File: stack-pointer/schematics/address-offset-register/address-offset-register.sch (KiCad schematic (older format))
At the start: 12 parts

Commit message: more work on stack pointer
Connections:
- net GND: no longer U?.7 (C0)
- new net AP1: U?.7 (C0)
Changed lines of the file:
@@
 	1    0    0    -1
 $EndComp
-$Comp
-L common-symbols:BarGraphLED_8P BAR?
-U 1 1 615D5CEB
-P 10350 3675
-F 0 "BAR?" H 10350 4342 50  0000 C CNN
-F 1 "BarGraphLED_8P" H 10350 4251 50  0000 C CNN
-F 2 "" H 10350 3675 50  0001 C CNN
-F 3 "" H 10350 3675 50  0001 C CNN
-	1    10350 3675
-	1    0    0    -1
-$EndComp
-Wire Wire Line
-	10150 3975 10050 3975
 Connection ~ 8625 3975
 Wire Wire Line
 	8625 3975 8625 4150
-Wire Wire Line
-	10150 3875 9950 3875
 Connection ~ 8525 3875
 Wire Wire Line
 	8525 3875 8525 3225
-Wire Wire Line
-	10150 3775 9850 3775
 Connection ~ 8425 3775
 Wire Wire Line
 	8425 3775 8425 4150
-Wire Wire Line
-	10150 3675 9750 3675
 Connection ~ 8325 3675
 Wire Wire Line
 	8325 3675 8325 3225
-Wire Wire Line
-	10150 3575 9650 3575
 Connection ~ 6650 3575
 Wire Wire Line
 	6650 3575 6650 3225
-Wire Wire Line
-	10150 3475 9550 3475
 Connection ~ 6550 3475
 Wire Wire Line
 	6550 3475 6550 3225
-Wire Wire Line
-	10150 3375 9450 3375
 Connection ~ 6450 3375
 Wire Wire Line
 	6450 3375 6450 3225
-Wire Wire Line
-	10150 3275 9350 3275
 Connection ~ 6350 3275
 Wire Wire Line
@@
 Text HLabel 9450 2200 2    50   Input ~ 0
 AOa
+Wire Wire Line
+	7825 3675 7825 4150
+Wire Wire Line
+	9350 2200 9450 2200
+Wire Wire Line
+	8750 2200 8125 2200
+Connection ~ 8125 2200
+Wire Wire Line
+	6575 6025 6575 6150
+Wire Wire Line
+	6475 5950 6475 6150
+Wire Wire Line
+	6375 5875 6375 6150
+Wire Wire Line
+	6275 5800 6275 6150
+Wire Wire Line
+	6175 5725 6175 6150
+Wire Wire Line
+	6075 5650 6075 6150
+Wire Wire Line
+	5975 5575 5975 6150
+Wire Wire Line
+	5875 5500 5875 6150
+$Comp
+L power:GND #PWR?
+U 1 1 61603AA0
+P 10050 4475
+F 0 "#PWR?" H 10050 4225 50  0001 C CNN
+F 1 "GND" H 10055 4302 50  0000 C CNN
+F 2 "" H 10050 4475 50  0001 C CNN
+F 3 "" H 10050 4475 50  0001 C CNN
+	1    10050 4475
+	1    0    0    -1
+$EndComp
+Wire Wire Line
+	10050 3975 8625 3975
+Wire Wire Line
+	10150 3975 10050 3975
+Connection ~ 10050 3975
+Wire Wire Line
+	10050 4075 10050 3975
+Wire Wire Line
+	9950 3875 8525 3875
+Wire Wire Line
+	10150 3875 9950 3875
+Connection ~ 9950 3875
+Wire Wire Line
+	9950 4075 9950 3875
+Wire Wire Line
+	9850 3775 8425 3775
+Wire Wire Line
+	10150 3775 9850 3775
+Connection ~ 9850 3775
+Wire Wire Line
+	9850 4075 9850 3775
+Wire Wire Line
+	9750 3675 8325 3675
+Wire Wire Line
+	10150 3675 9750 3675
+Connection ~ 9750 3675
+Wire Wire Line
+	9750 4075 9750 3675
+Wire Wire Line
+	9650 3575 6650 3575
+Wire Wire Line
+	10150 3575 9650 3575
+Connection ~ 9650 3575
+Wire Wire Line
+	9650 4075 9650 3575
+Wire Wire Line
+	9550 3475 6550 3475
+Wire Wire Line
+	10150 3475 9550 3475
+Connection ~ 9550 3475
+Wire Wire Line
+	9550 4075 9550 3475
+Wire Wire Line
+	9450 3375 6450 3375
+Wire Wire Line
+	10150 3375 9450 3375
+Connection ~ 9450 3375
+Wire Wire Line
+	9450 4075 9450 3375
+Wire Wire Line
+	9350 3275 6350 3275
+Wire Wire Line
+	10150 3275 9350 3275
+Connection ~ 9350 3275
+Wire Wire Line
+	9350 4075 9350 3275
+$Comp
+L common-symbols:BarGraphLED_8P BAR?
+U 1 1 615D5CEB
+P 10350 3675
+F 0 "BAR?" H 10350 4342 50  0000 C CNN
+F 1 "BarGraphLED_8P" H 10350 4251 50  0000 C CNN
+F 2 "" H 10350 3675 50  0001 C CNN
+F 3 "" H 10350 3675 50  0001 C CNN
+	1    10350 3675
+	1    0    0    -1
+$EndComp
 $Comp
 L Device:R_Network08_US RN?
@@
 	-1   0    0    1
 $EndComp
-Wire Wire Line
-	10050 4075 10050 3975
-Connection ~ 10050 3975
-Wire Wire Line
-	10050 3975 8625 3975
-Wire Wire Line
-	9950 4075 9950 3875
-Connection ~ 9950 3875
-Wire Wire Line
-	9950 3875 8525 3875
-Wire Wire Line
-	9850 4075 9850 3775
-Connection ~ 9850 3775
-Wire Wire Line
-	9850 3775 8425 3775
-Wire Wire Line
-	9750 4075 9750 3675
-Connection ~ 9750 3675
-Wire Wire Line
-	9750 3675 8325 3675
-Wire Wire Line
-	9650 4075 9650 3575
-Connection ~ 9650 3575
-Wire Wire Line
-	9650 3575 6650 3575
-Wire Wire Line
-	9550 4075 9550 3475
-Connection ~ 9550 3475
-Wire Wire Line
-	9550 3475 6550 3475
-Wire Wire Line
-	9450 4075 9450 3375
-Connection ~ 9450 3375
-Wire Wire Line
-	9450 3375 6450 3375
-Wire Wire Line
-	9350 4075 9350 3275
-Connection ~ 9350 3275
-Wire Wire Line
-	9350 3275 6350 3275
-$Comp
-L power:GND #PWR?
-U 1 1 61603AA0
-P 10050 4475
-F 0 "#PWR?" H 10050 4225 50  0001 C CNN
-F 1 "GND" H 10055 4302 50  0000 C CNN
-F 2 "" H 10050 4475 50  0001 C CNN
-F 3 "" H 10050 4475 50  0001 C CNN
-	1    10050 4475
-	1    0    0    -1
-$EndComp
-Wire Wire Line
-	7825 3675 7825 4150
-Wire Wire Line
-	8825 4150 8825 4075
-Wire Wire Line
-	8825 4075 7525 4075
-Wire Wire Line
-	7525 4075 7525 4650
-Connection ~ 7525 4650
-Wire Wire Line
-	9350 2200 9450 2200
-Wire Wire Line
-	8750 2200 8125 2200
-Connection ~ 8125 2200
-Wire Wire Line
-	6575 6025 6575 6150
-Wire Wire Line
-	6475 5950 6475 6150
-Wire Wire Line
-	6375 5875 6375 6150
-Wire Wire Line
-	6275 5800 6275 6150
-Wire Wire Line
-	6175 5725 6175 6150
-Wire Wire Line
-	6075 5650 6075 6150
-Wire Wire Line
-	5975 5575 5975 6150
-Wire Wire Line
-	5875 5500 5875 6150
+Text HLabel 9450 2875 2    50   Input ~ 0
+AP1
+Wire Wire Line
+	8825 2875 9450 2875
+Wire Wire Line
+	8825 2875 8825 4150
 $EndSCHEMATC

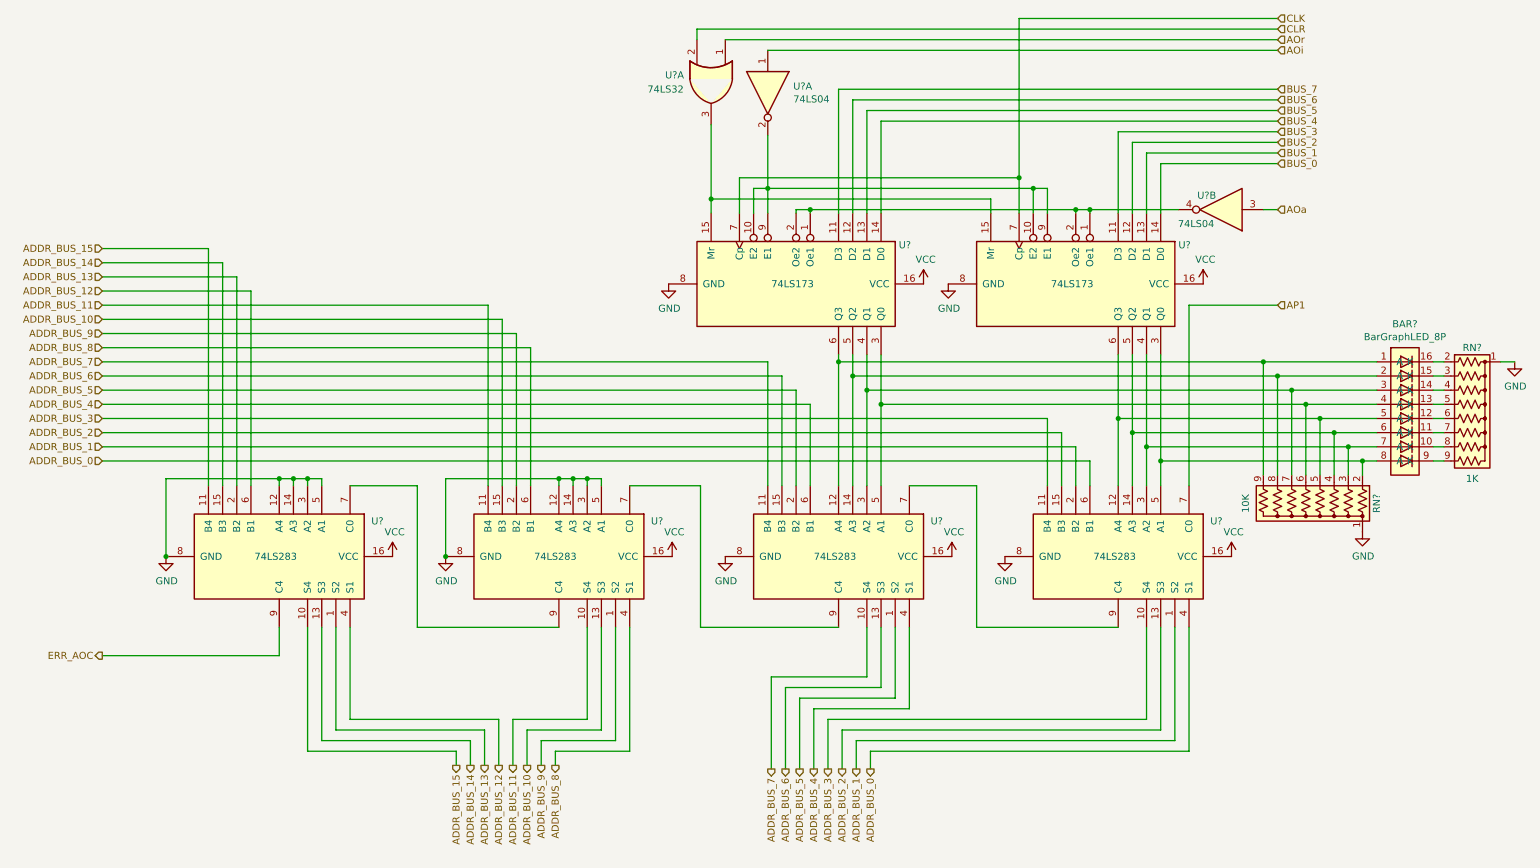
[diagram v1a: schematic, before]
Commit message: updated address bus handling and added support for halt on error
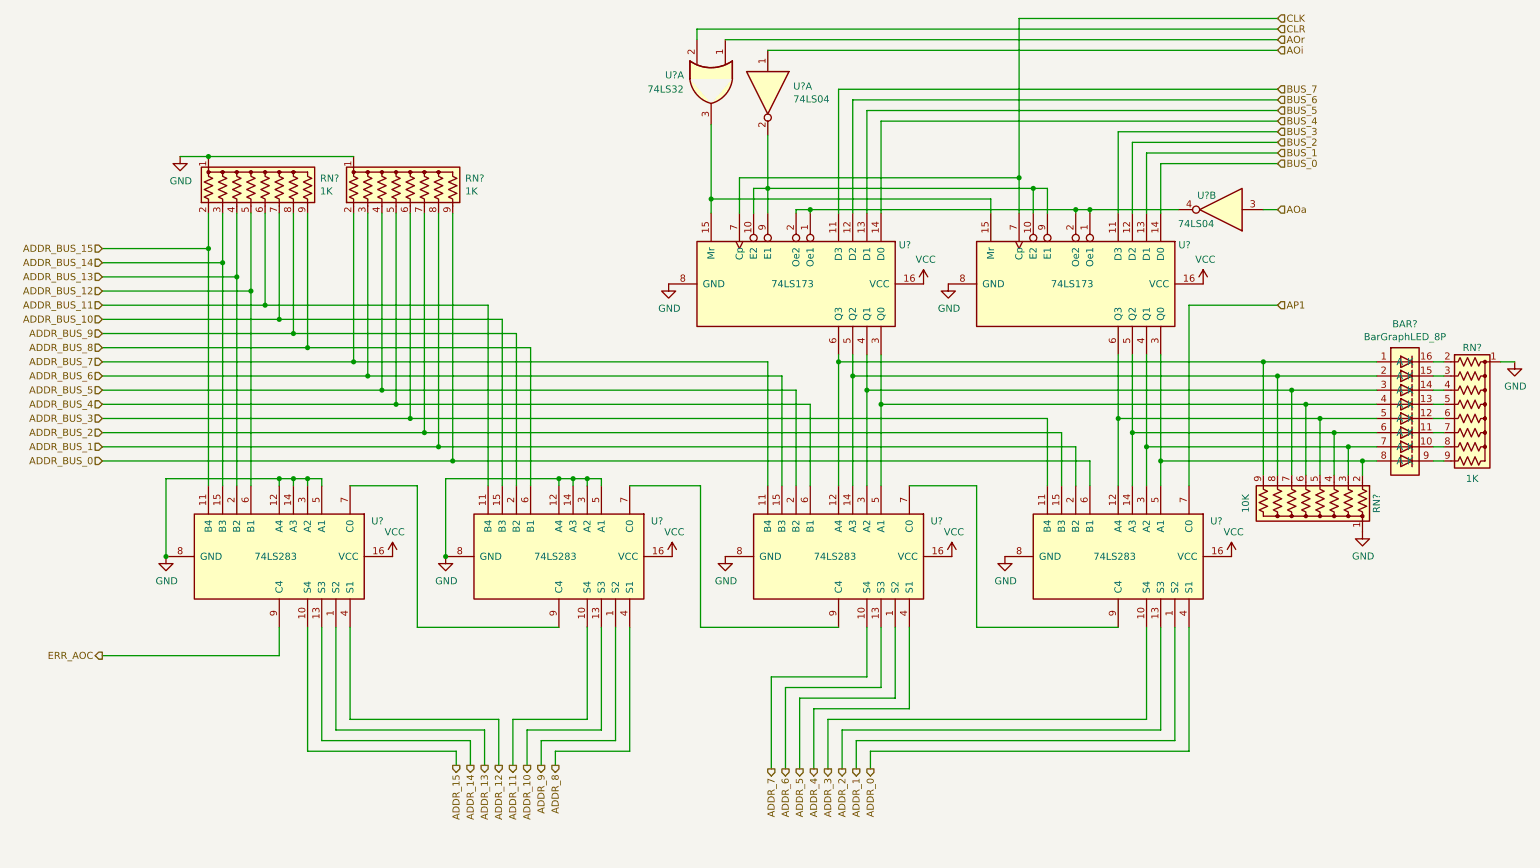
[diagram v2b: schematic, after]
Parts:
- added RN? (x2): 1K, Resistor_THT:R_Array_SIP9, symbol Device:R_Network08_US
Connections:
- net ADDR_BUS_0: now also RN?.9 (R8); no longer U?.4 (S1)
- net ADDR_BUS_1: now also RN?.8 (R7); no longer U?.1 (S2)
- net ADDR_BUS_10: now also RN?.7 (R6); no longer U?.13 (S3)
- net ADDR_BUS_11: now also RN?.6 (R5); no longer U?.10 (S4)
- net ADDR_BUS_12: now also RN?.5 (R4); no longer U?.4 (S1)
- net ADDR_BUS_13: now also RN?.4 (R3); no longer U?.1 (S2)
- net ADDR_BUS_14: now also RN?.3 (R2); no longer U?.13 (S3)
- net ADDR_BUS_15: now also RN?.2 (R1); no longer U?.10 (S4)
- net ADDR_BUS_2: now also RN?.7 (R6); no longer U?.13 (S3)
- net ADDR_BUS_3: now also RN?.6 (R5); no longer U?.10 (S4)
- net ADDR_BUS_4: now also RN?.5 (R4); no longer U?.4 (S1)
- net ADDR_BUS_5: now also RN?.4 (R3); no longer U?.1 (S2)
- net ADDR_BUS_6: now also RN?.3 (R2); no longer U?.13 (S3)
- net ADDR_BUS_7: now also RN?.2 (R1); no longer U?.10 (S4)
- net ADDR_BUS_8: now also RN?.9 (R8); no longer U?.4 (S1)
- net ADDR_BUS_9: now also RN?.8 (R7); no longer U?.1 (S2)
- net GND: now also RN?.1 (common), RN?.1 (common)
- new net ADDR_0: U?.4 (S1)
- new net ADDR_1: U?.1 (S2)
- new net ADDR_10: U?.13 (S3)
- new net ADDR_11: U?.10 (S4)
- new net ADDR_12: U?.4 (S1)
- new net ADDR_13: U?.1 (S2)
- new net ADDR_14: U?.13 (S3)
- new net ADDR_15: U?.10 (S4)
- new net ADDR_2: U?.13 (S3)
- new net ADDR_3: U?.10 (S4)
- new net ADDR_4: U?.4 (S1)
- new net ADDR_5: U?.1 (S2)
- new net ADDR_6: U?.13 (S3)
- new net ADDR_7: U?.10 (S4)
- new net ADDR_8: U?.4 (S1)
- new net ADDR_9: U?.1 (S2)
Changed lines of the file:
@@
 	6350 1350 6350 2225
 Text HLabel 6575 6150 3    50   Output ~ 0
-ADDR_BUS_0
+ADDR_0
 Text HLabel 6475 6150 3    50   Output ~ 0
-ADDR_BUS_1
+ADDR_1
 Text HLabel 6375 6150 3    50   Output ~ 0
-ADDR_BUS_2
+ADDR_2
 Text HLabel 6275 6150 3    50   Output ~ 0
-ADDR_BUS_3
+ADDR_3
 Text HLabel 6175 6150 3    50   Output ~ 0
-ADDR_BUS_4
+ADDR_4
 Text HLabel 6075 6150 3    50   Output ~ 0
-ADDR_BUS_5
+ADDR_5
 Text HLabel 5975 6150 3    50   Output ~ 0
-ADDR_BUS_6
+ADDR_6
 Text HLabel 5875 6150 3    50   Output ~ 0
-ADDR_BUS_7
+ADDR_7
 Text HLabel 4350 6125 3    50   Output ~ 0
-ADDR_BUS_8
+ADDR_8
 Text HLabel 4250 6125 3    50   Output ~ 0
-ADDR_BUS_9
+ADDR_9
 Text HLabel 4150 6125 3    50   Output ~ 0
-ADDR_BUS_10
+ADDR_10
 Text HLabel 4050 6125 3    50   Output ~ 0
-ADDR_BUS_11
+ADDR_11
 Text HLabel 3950 6125 3    50   Output ~ 0
-ADDR_BUS_12
+ADDR_12
 Text HLabel 3850 6125 3    50   Output ~ 0
-ADDR_BUS_13
+ADDR_13
 Text HLabel 3750 6125 3    50   Output ~ 0
-ADDR_BUS_14
+ADDR_14
 Text HLabel 3650 6125 3    50   Output ~ 0
-ADDR_BUS_15
+ADDR_15
 Wire Wire Line
 	4375 4150 4375 4100
@@
 ADDR_BUS_1
 Wire Wire Line
-	1150 3875 8025 3875
+	1150 3875 3525 3875
 Wire Wire Line
 	8025 3875 8025 4150
@@
 ADDR_BUS_7
 Wire Wire Line
-	1150 3975 8125 3975
+	1150 3975 3625 3975
 Wire Wire Line
 	8125 3975 8125 4150
 Wire Wire Line
-	1150 3775 7925 3775
+	1150 3775 3425 3775
 Wire Wire Line
 	7925 3775 7925 4150
 Wire Wire Line
-	1150 3675 7825 3675
-Wire Wire Line
-	1150 3575 6150 3575
+	1150 3675 3325 3675
+Wire Wire Line
+	1150 3575 3225 3575
 Wire Wire Line
 	6150 3575 6150 4150
 Wire Wire Line
-	1150 3475 6050 3475
+	1150 3475 3125 3475
 Wire Wire Line
 	6050 3475 6050 4150
 Wire Wire Line
-	1150 3375 5950 3375
+	1150 3375 3025 3375
 Wire Wire Line
 	5950 3375 5950 4150
 Wire Wire Line
-	1150 3275 5850 3275
+	1150 3275 2925 3275
 Wire Wire Line
 	5850 3275 5850 4150
@@
 ADDR_BUS_15
 Wire Wire Line
-	1150 3175 4175 3175
+	1150 3175 2600 3175
 Wire Wire Line
 	4175 3175 4175 4150
 Wire Wire Line
-	1150 3075 4075 3075
+	1150 3075 2500 3075
 Wire Wire Line
 	4075 3075 4075 4150
 Wire Wire Line
-	1150 2975 3975 2975
+	1150 2975 2400 2975
 Wire Wire Line
 	3975 2975 3975 4150
 Wire Wire Line
-	1150 2875 3875 2875
+	1150 2875 2300 2875
 Wire Wire Line
 	3875 2875 3875 4150
@@
 Wire Wire Line
 	8825 2875 8825 4150
+$Comp
+L Device:R_Network08_US RN?
+U 1 1 6161A5EE
+P 2300 2025
+F 0 "RN?" H 2688 2071 50  0000 L CNN
+F 1 "1K" H 2688 1980 50  0000 L CNN
+F 2 "Resistor_THT:R_Array_SIP9" V 2775 2025 50  0001 C CNN
+F 3 "http://www.vishay.com/docs/31509/csc.pdf" H 2300 2025 50  0001 C CNN
+	1    2300 2025
+	1    0    0    -1
+$EndComp
+$Comp
+L Device:R_Network08_US RN?
+U 1 1 6161C78B
+P 3325 2025
+F 0 "RN?" H 3713 2071 50  0000 L CNN
+F 1 "1K" H 3713 1980 50  0000 L CNN
+F 2 "Resistor_THT:R_Array_SIP9" V 3800 2025 50  0001 C CNN
+F 3 "http://www.vishay.com/docs/31509/csc.pdf" H 3325 2025 50  0001 C CNN
+	1    3325 2025
+	1    0    0    -1
+$EndComp
+Wire Wire Line
+	1900 2225 1900 2475
+Connection ~ 1900 2475
+Wire Wire Line
+	2000 2575 2000 2225
+Connection ~ 2000 2575
+Wire Wire Line
+	2100 2225 2100 2675
+Connection ~ 2100 2675
+Wire Wire Line
+	2200 2225 2200 2775
+Connection ~ 2200 2775
+Wire Wire Line
+	2300 2225 2300 2875
+Connection ~ 2300 2875
+Wire Wire Line
+	2300 2875 3875 2875
+Wire Wire Line
+	2400 2225 2400 2975
+Connection ~ 2400 2975
+Wire Wire Line
+	2400 2975 3975 2975
+Wire Wire Line
+	2500 2225 2500 3075
+Connection ~ 2500 3075
+Wire Wire Line
+	2500 3075 4075 3075
+Wire Wire Line
+	2600 2225 2600 3175
+Connection ~ 2600 3175
+Wire Wire Line
+	2600 3175 4175 3175
+Wire Wire Line
+	2925 2225 2925 3275
+Connection ~ 2925 3275
+Wire Wire Line
+	2925 3275 5850 3275
+Wire Wire Line
+	3025 2225 3025 3375
+Connection ~ 3025 3375
+Wire Wire Line
+	3025 3375 5950 3375
+Wire Wire Line
+	3125 2225 3125 3475
+Connection ~ 3125 3475
+Wire Wire Line
+	3125 3475 6050 3475
+Wire Wire Line
+	3225 2225 3225 3575
+Connection ~ 3225 3575
+Wire Wire Line
+	3225 3575 6150 3575
+Wire Wire Line
+	3325 2225 3325 3675
+Connection ~ 3325 3675
+Wire Wire Line
+	3325 3675 7825 3675
+Wire Wire Line
+	3425 2225 3425 3775
+Connection ~ 3425 3775
+Wire Wire Line
+	3425 3775 7925 3775
+Wire Wire Line
+	3525 2225 3525 3875
+Connection ~ 3525 3875
+Wire Wire Line
+	3525 3875 8025 3875
+Wire Wire Line
+	3625 2225 3625 3975
+Connection ~ 3625 3975
+Wire Wire Line
+	3625 3975 8125 3975
+Wire Wire Line
+	2925 1825 1900 1825
+$Comp
+L power:GND #PWR?
+U 1 1 6170BD34
+P 1700 1825
+F 0 "#PWR?" H 1700 1575 50  0001 C CNN
+F 1 "GND" H 1705 1652 50  0000 C CNN
+F 2 "" H 1700 1825 50  0001 C CNN
+F 3 "" H 1700 1825 50  0001 C CNN
+	1    1700 1825
+	1    0    0    -1
+$EndComp
+Wire Wire Line
+	1700 1825 1900 1825
+Connection ~ 1900 1825
 $EndSCHEMATC

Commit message: small iteration on schematics
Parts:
- removed U?: 74LS32, symbol 74xx:74LS32
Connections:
- net CLR: now also U?.15 (Mr), U?.15 (Mr)
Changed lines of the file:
@@
 Text HLabel 9450 1075 2    50   Input ~ 0
 AOi
-Text HLabel 9450 1000 2    50   Input ~ 0
-AOr
 Text HLabel 9450 925  2    50   Input ~ 0
 CLR
-$Comp
-L 74xx:74LS32 U?
-U 1 1 61681F6C
-P 5450 1300
-F 0 "U?" V 5400 975 50  0000 L CNN
-F 1 "74LS32" V 5500 850 50  0000 L CNN
-F 2 "" H 5450 1300 50  0001 C CNN
-F 3 "http://www.ti.com/lit/gpn/sn74LS32" H 5450 1300 50  0001 C CNN
-	1    5450 1300
-	0    1    1    0
-$EndComp
-Wire Wire Line
-	5550 1000 9450 1000
-Wire Wire Line
-	9450 925  5350 925
-Wire Wire Line
-	5350 925  5350 1000
-Wire Wire Line
-	5450 1600 5450 2125
 Wire Wire Line
 	7425 2225 7425 2125
@@
 	1700 1825 1900 1825
 Connection ~ 1900 1825
+Wire Wire Line
+	9450 925  5450 925
+Wire Wire Line
+	5450 925  5450 2125
 $EndSCHEMATC

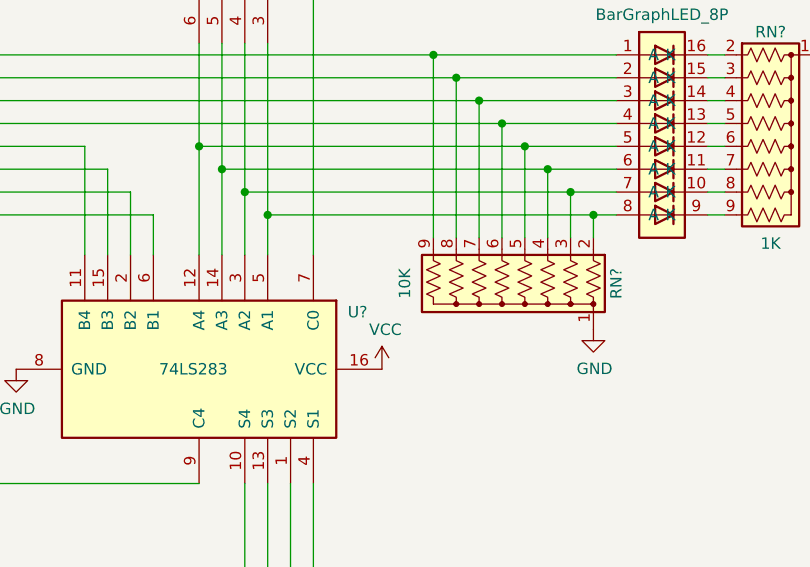
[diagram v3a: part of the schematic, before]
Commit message: updated pull down resistor value
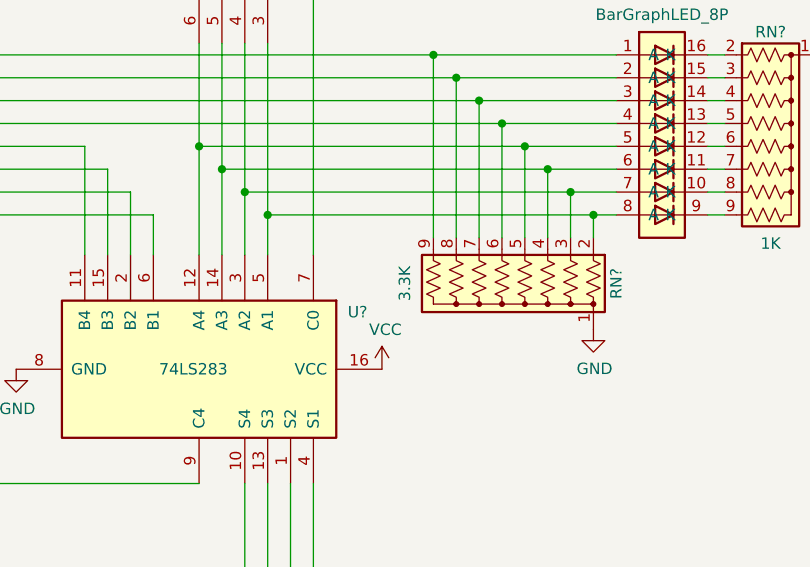
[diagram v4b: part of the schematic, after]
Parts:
- RN?: value 10K -> 3.3K
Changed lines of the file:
@@
 P 9650 4275
 F 0 "RN?" V 9150 4275 50  0000 C CNN
-F 1 "10K" V 10075 4275 50  0000 C CNN
+F 1 "3.3K" V 10075 4275 50  0000 C CNN
 F 2 "Resistor_THT:R_Array_SIP9" V 10125 4275 50  0001 C CNN
 F 3 "http://www.vishay.com/docs/31509/csc.pdf" H 9650 4275 50  0001 C CNN
